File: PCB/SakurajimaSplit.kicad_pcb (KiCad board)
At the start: 2 copper layers, 226 parts, among them J1 SWD, J10 Conn_01x01_Pin, J11 Conn_01x01_Pin, J12 Conn_01x01_Pin, J13 Conn_01x01_Pin, J14 Conn_01x01_Pin, J15 Conn_01x01_Pin, J16 Conn_01x01_Pin, J17 Conn_01x01_Pin, J18 Conn_01x01_Pin, J19 USB-C to Host, J2 USB-C to Right-Half, J20 SWD, J21 Conn_01x01_Pin, J22 Conn_01x01_Pin, J23 Conn_01x01_Pin, J24 Conn_01x01_Pin, J25 Conn_01x01_Pin, J26 Conn_01x01_Pin, J27 Conn_01x01_Pin, J28 Conn_01x01_Pin, J29 Conn_01x01_Pin, J3 Conn_01x01_Pin, J30 Conn_01x01_Pin, J31 Conn_01x01_Pin, J32 Conn_01x01_Pin, J33 Conn_01x01_Pin, J34 Conn_01x01_Pin, J35 Conn_01x01_Pin, J36 Conn_01x01_Pin, J37 Conn_01x01_Pin, J38 Conn_01x01_Pin, J39 USB-C to Right-Half, J4 Conn_01x01_Pin, J5 Conn_01x01_Pin, J6 Conn_01x01_Pin, J7 Conn_01x01_Pin, J8 Conn_01x01_Pin, J9 Conn_01x01_Pin, SW1 SWCLK/BOOT0, SW2 Knob, SW3 SWCLK/BOOT0, SW4 Knob, U1 USBLC6-2SC6, U2 STM32G0B1CBT6, U3 ZJY_M233, U4 TLV76733DRVR, U5 USBLC6-2SC6, U6 STM32G0B1CBT6, U7 ZJY_M233, U8 TLV76733DRVR, U9 USBLC6-2SC6, Y1 8MHz, Y2 8MHz

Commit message: feat(pcb): design rough layout and update schematic accordingly
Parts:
- removed C17, C18, C19: 100nF, Capacitor_SMD:C_0603_1608Metric
- removed C20: TBD, Capacitor_SMD:C_0805_2012Metric
- removed C21, C22: 4.7uF, Capacitor_SMD:C_0805_2012Metric
- removed J10, J11, J12, J13, J14, J32, J33, J34, J38, J4, J5, J6, J7, J8, J9: Conn_01x01_Pin, Connector_Wire:SolderWirePad_1x01_SMD_1x2mm
- removed J39: USB-C to Right-Half, Connector_USB:USB_C_Receptacle_G-Switch_GT-USB-7010ASV
- removed R13: TBD, Resistor_SMD:R_0603_1608Metric
- removed R14, R15, R16, R17, R18, R19: 10k, Resistor_SMD:R_0603_1608Metric
- removed R20: 330R, Resistor_SMD:R_0603_1608Metric
- removed SW3: SWCLK/BOOT0, Button_Switch_SMD:SW_Push_1P1T_XKB_TS-1187A
- removed SW4: Knob, Rotary_Encoder:RotaryEncoder_Alps_EC11E-Switch_Vertical_H20mm
- removed TP3, TP5, TP6: GND, TestPoint:TestPoint_Pad_2.0x2.0mm
- added TP25: Flash_SDO, Hayata_Lib:TestPoint_Pad_Circular_1.3mm, B.Cu at (161.9, 123.8)
- added TP26: Display_SCLK, Hayata_Lib:TestPoint_Pad_Circular_1.3mm, F.Cu at (165.1, 161.1)
- added TP27: Display_SDI, Hayata_Lib:TestPoint_Pad_Circular_1.3mm, F.Cu at (167.5, 161.1)
- added TP28: Flash_SDO, Hayata_Lib:TestPoint_Pad_Circular_1.3mm, F.Cu at (509.5, 111.2)
- added TP29: Display_SCLK, Hayata_Lib:TestPoint_Pad_Circular_1.3mm, F.Cu at (509.5, 114.7)
- added TP30: Display_SDI, Hayata_Lib:TestPoint_Pad_Circular_1.3mm, F.Cu at (509.5, 118.1)
- added U10: ZJY_M233, Hayata_Lib:OLED_SSD1305, F.Cu at (166.5, 133.5)
- added U11: ZJY_M233, Hayata_Lib:OLED_SSD1305, F.Cu at (479.8, 146.6)
- C1, C6, C7: value 100nF -> 20pF; footprint Capacitor_SMD:C_0603_1608Metric -> Capacitor_SMD:C_0402_1005Metric_Pad0.74x0.62mm_HandSolder
- C13: value 20pF -> 100nF; footprint Capacitor_SMD:C_0402_1005Metric_Pad0.74x0.62mm_HandSolder -> Capacitor_SMD:C_0603_1608Metric
- C14: value 20pF -> TBD; footprint Capacitor_SMD:C_0402_1005Metric_Pad0.74x0.62mm_HandSolder -> Capacitor_SMD:C_0805_2012Metric
- C16, C8: value 100nF -> 4.7uF; footprint Capacitor_SMD:C_0603_1608Metric -> Capacitor_SMD:C_0805_2012Metric
- C3: value 20pF -> 4.7uF; footprint Capacitor_SMD:C_0402_1005Metric_Pad0.74x0.62mm_HandSolder -> Capacitor_SMD:C_0805_2012Metric
- C4: value 4.7uF -> 100nF; footprint Capacitor_SMD:C_0805_2012Metric -> Capacitor_SMD:C_0603_1608Metric
- C5, D1, D10, D11, D12, D13, D14, D15, D16, D17, D18, D19, D2, D20, D21, D3, D4, D5, D6, D7, D8, D9, J1: moved to B.Cu
- H1, H2, H3, H4, H5, H6, H7, H8: footprint MountingHole:MountingHole_3.2mm_M3_Pad -> MountingHole:MountingHole_3.2mm_M3_Pad_Via
- J15: value Conn_01x01_Pin -> SWD; footprint Connector_Wire:SolderWirePad_1x01_SMD_1x2mm -> Connector_PinHeader_2.54mm:PinHeader_1x05_P2.54mm_Horizontal
- J20: value SWD -> Conn_01x01_Pin; footprint Connector_PinHeader_2.54mm:PinHeader_1x05_P2.54mm_Horizontal -> Connector_Wire:SolderWirePad_1x01_SMD_1x2mm
- J3: value Conn_01x01_Pin -> VREF+
- J31: value Conn_01x01_Pin -> USB-C to Right-Half; footprint Connector_Wire:SolderWirePad_1x01_SMD_1x2mm -> Connector_USB:USB_C_Receptacle_G-Switch_GT-USB-7010ASV
- MX21, MX40: footprint PCM_marbastlib-mx:SW_MX_1u -> PCM_marbastlib-mx:SW_MX_1.5u
- R3, R4: value 10k -> 5.1k; moved to B.Cu
- R5: value 10k -> 330R
- R6: value 10k -> TBD
- R7, R8: value 10k -> 5.1k
- SW1: footprint Button_Switch_SMD:SW_Push_1P1T_XKB_TS-1187A -> Hayata_Lib:SW_Push_TS-1010B
- SW2: value Knob -> SWCLK/BOOT0; footprint Rotary_Encoder:RotaryEncoder_Alps_EC11E-Switch_Vertical_H20mm -> Hayata_Lib:SW_Push_TS-1010B
- TP1, TP10, TP11, TP12, TP13, TP14, TP15, TP16, TP17, TP2, TP20, TP21, TP22, TP23, TP24, TP4, TP9: footprint TestPoint:TestPoint_Pad_2.0x2.0mm -> Hayata_Lib:TestPoint_Pad_Circular_1.3mm
- TP18: value Display_SCLK -> Flash_SCLK; footprint TestPoint:TestPoint_Pad_2.0x2.0mm -> Hayata_Lib:TestPoint_Pad_Circular_1.3mm
- TP19: value Display_SDI -> Flash_SDI; footprint TestPoint:TestPoint_Pad_2.0x2.0mm -> Hayata_Lib:TestPoint_Pad_Circular_1.3mm
- TP7: value Display_SCLK -> Flash_SCLK; footprint TestPoint:TestPoint_Pad_2.0x2.0mm -> Hayata_Lib:TestPoint_Pad_Circular_1.3mm; moved to B.Cu
- TP8: value Display_SDI -> Flash_SDI; footprint TestPoint:TestPoint_Pad_2.0x2.0mm -> Hayata_Lib:TestPoint_Pad_Circular_1.3mm; moved to B.Cu
- U3: value ZJY_M233 -> W25Q128JVS; footprint Hayata_Lib:OLED_SSD1305 -> Package_SO:SOIC-8_5.3x5.3mm_P1.27mm; moved to B.Cu
- U7: value ZJY_M233 -> W25Q128JVS; footprint Hayata_Lib:OLED_SSD1305 -> Package_SO:SOIC-8_5.3x5.3mm_P1.27mm
- Y1, Y2: footprint Crystal:Crystal_SMD_3225-4Pin_3.2x2.5mm_HandSoldering -> Crystal:Crystal_SMD_3225-4Pin_3.2x2.5mm
- moved SW2 586.0 mm to (504.8, 130.5)
- moved C6 553.4 mm to (507.7, 136.4)
- moved C7 553.4 mm to (507.7, 138.4)
- moved C8 548.6 mm to (503.1, 138.9)
- moved J15 539.9 mm to (499.2, 154.2)
- moved R5 537.6 mm to (494.9, 158.2)
- moved R6 534.7 mm to (494.9, 160.7)
- moved R7 534.7 mm to (494.9, 163.2)
- moved R8 534.7 mm to (494.9, 165.7)
- moved J18 533.3 mm to (499.3, 143.1)
- moved J17 533.1 mm to (496.8, 143.1)
- moved J16 532.9 mm to (494.2, 143.1)
- moved H1 247.4 mm to (196.1, 122.2)
- moved H2 247.4 mm to (196.1, 130.1)
- moved H3 247.4 mm to (196.1, 138.1)
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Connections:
- C1 pad 1: +3.3V -> /Left-Half/HSE_IN
- C1 pad 2: /Left-Half/SWCLK/BOOT0 -> GND
- C12 pad 2: /Right-Half/SWCLK/BOOT0 -> GND
- C13 pad 1: /Right-Half/HSE_IN -> +3.3V
- C14 pad 1: Net-(C14-Pad1) -> Net-(JP3-B)
- C15 pad 1: +3.3V -> +5V
- C16 pad 1: +3.3V -> Net-(D47-A)
- C2 pad 1: /Left-Half/HSE_IN -> Net-(C2-Pad1)
- C3 pad 1: Net-(C3-Pad1) -> +3.3V
- C6 pad 1: /Left-Half/Knob_A -> /Right-Half/HSE_IN
- C7 pad 1: /Left-Half/Knob_B -> Net-(C7-Pad1)
- C8 pad 1: /Left-Half/Knob_SW -> +3.3V
- D43 pad 1: Net-(D43-K) -> GND
- D43 pad 2: /Left-Half/CapsLock -> Net-(D43-A)
- D45 pad 1: Net-(D45-K) -> GND
- D45 pad 2: Net-(D44-A) -> Net-(D45-A)
- D46 pad 1: Net-(D46-K) -> GND
- D46 pad 2: /Right-Half/CapsLock -> Net-(D46-A)
- D48 pad 1: Net-(D48-K) -> GND
- D48 pad 2: Net-(D47-A) -> Net-(D48-A)
- J15 pad 1: Net-(J15-Pin_1) -> +3.3V
- J20 pad 1: +3.3V -> Net-(J20-Pin_1)
- R1 pad 1: Net-(D43-K) -> /Left-Half/CapsLock
- R1 pad 2: GND -> Net-(D43-A)
- R11 pad 1: Net-(D45-K) -> Net-(D44-A)
- R11 pad 2: GND -> Net-(D45-A)
- R12 pad 1: Net-(D46-K) -> Net-(D47-A)
- R12 pad 2: GND -> Net-(D48-A)
- R2 pad 1: Net-(C3-Pad1) -> Net-(C2-Pad1)
- R3 pad 1: Net-(R3-Pad1) -> +3.3V
- R3 pad 2: +3.3V -> /Left-Half/Flash_~{CS}
- R4 pad 1: Net-(R4-Pad1) -> +3.3V
- R4 pad 2: +3.3V -> Net-(U3-~{HOLD}/~{RESET}/IO_{3})
- R5 pad 1: Net-(R5-Pad1) -> /Right-Half/CapsLock
- R5 pad 2: +3.3V -> Net-(D46-A)
- R6 pad 1: /Left-Half/Knob_A -> Net-(C7-Pad1)
- R6 pad 2: Net-(R3-Pad1) -> /Right-Half/HSE_OUT
- R7 pad 1: /Left-Half/Knob_B -> +3.3V
- R7 pad 2: Net-(R4-Pad1) -> /Right-Half/Flash_~{CS}
- R8 pad 1: /Left-Half/Knob_SW -> +3.3V
- R8 pad 2: Net-(R5-Pad1) -> Net-(U7-~{HOLD}/~{RESET}/IO_{3})
- TP18 pad 1: /Right-Half/Display_SCLK -> /Right-Half/Flash_SCLK
- TP19 pad 1: /Right-Half/Display_SDI -> /Right-Half/Flash_SDI
- TP20 pad 1: VBUS -> Net-(JP3-B)
- TP7 pad 1: /Left-Half/Display_SCLK -> /Left-Half/Flash_SCLK
- TP8 pad 1: /Left-Half/Display_SDI -> /Left-Half/Flash_SDI
- TP9 pad 1: VBUS -> Net-(JP1-B)
- U2 pad 1: /Left-Half/Knob_A -> /Left-Half/Display_~{CS}
- U2 pad 11: Net-(J4-Pin_1) -> unconnected-(U2-PA0-Pad11)
- U2 pad 12: Net-(J5-Pin_1) -> unconnected-(U2-PA1-Pad12)
- U2 pad 15: Net-(J6-Pin_1) -> /Left-Half/CapsLock
- U2 pad 16: Net-(J7-Pin_1) -> unconnected-(U2-PA5-Pad16)
- U2 pad 17: Net-(J8-Pin_1) -> unconnected-(U2-PA6-Pad17)
- U2 pad 18: Net-(J9-Pin_1) -> unconnected-(U2-PA7-Pad18)
- U2 pad 19: Net-(J16-Pin_1) -> unconnected-(U2-PB0-Pad19)
- U2 pad 2: /Left-Half/Knob_B -> /Left-Half/Display_~{RST}
- U2 pad 20: /Left-Half/CapsLock -> unconnected-(U2-PB1-Pad20)
- U2 pad 21: /Left-Half/Display_DC -> unconnected-(U2-PB2-Pad21)
- U2 pad 22: /Left-Half/Display_~{RST} -> unconnected-(U2-PB10-Pad22)
- U2 pad 23: /Left-Half/Display_~{CS} -> unconnected-(U2-PB11-Pad23)
- U2 pad 24: /Left-Half/Display_~{EN} -> unconnected-(U2-PB12-Pad24)
- U2 pad 25: /Left-Half/Display_SCLK -> /Left-Half/COL0
- U2 pad 26: Net-(J18-Pin_1) -> /Left-Half/COL1
- U2 pad 27: /Left-Half/Display_SDI -> /Left-Half/COL2
- U2 pad 28: Net-(J10-Pin_1) -> /Left-Half/COL3
- U2 pad 29: Net-(J11-Pin_1) -> /Left-Half/COL4
- U2 pad 3: /Left-Half/Knob_SW -> /Left-Half/Display_DC
- U2 pad 30: Net-(J12-Pin_1) -> /Left-Half/COL5
- U2 pad 31: Net-(J13-Pin_1) -> unconnected-(U2-PC7-Pad31)
- U2 pad 32: Net-(J14-Pin_1) -> unconnected-(U2-PA10/UCPD1_DBCC2-Pad32)
- U2 pad 37: Net-(J15-Pin_1) -> /Left-Half/ROW0
- U2 pad 38: /Left-Half/ROW0 -> /Left-Half/ROW1
- U2 pad 39: /Left-Half/ROW1 -> /Left-Half/ROW2
- U2 pad 40: /Left-Half/ROW2 -> /Left-Half/ROW3
- U2 pad 41: /Left-Half/ROW3 -> /Left-Half/Flash_~{CS}
- U2 pad 42: Net-(J17-Pin_1) -> /Left-Half/Flash_SCLK
- U2 pad 43: /Left-Half/COL0 -> /Left-Half/Flash_SDO
- U2 pad 44: /Left-Half/COL1 -> /Left-Half/Flash_SDI
- U2 pad 45: /Left-Half/COL2 -> unconnected-(U2-PB6-Pad45)
- U2 pad 46: /Left-Half/COL3 -> /Left-Half/Display_SDI
- U2 pad 47: /Left-Half/COL4 -> /Left-Half/Display_SCLK
- U2 pad 48: /Left-Half/COL5 -> /Left-Half/Display_~{EN}
- U3 pad 1: GND -> /Left-Half/Flash_~{CS}
- U3 pad 2: +3.3V -> /Left-Half/Flash_SDO
- U3 pad 3: /Left-Half/Display_SCLK -> Net-(U3-~{HOLD}/~{RESET}/IO_{3})
- U3 pad 4: /Left-Half/Display_SDI -> GND
- U3 pad 5: /Left-Half/Display_~{RST} -> /Left-Half/Flash_SDI
- U3 pad 6: /Left-Half/Display_DC -> /Left-Half/Flash_SCLK
- U3 pad 7: /Left-Half/Display_~{CS} -> Net-(U3-~{HOLD}/~{RESET}/IO_{3})
- U3 pad 8: /Left-Half/Display_~{EN} -> +3.3V
- U6 pad 1: /Right-Half/Knob_A -> Net-(J27-Pin_1)
- U6 pad 11: Net-(J22-Pin_1) -> Net-(J17-Pin_1)
- U6 pad 12: Net-(J23-Pin_1) -> Net-(J18-Pin_1)
- U6 pad 15: Net-(J24-Pin_1) -> /Right-Half/Flash_~{CS}
- U6 pad 16: Net-(J25-Pin_1) -> /Right-Half/Flash_SCLK
- U6 pad 17: Net-(J26-Pin_1) -> /Right-Half/Flash_SDO
- U6 pad 18: Net-(J27-Pin_1) -> /Right-Half/Flash_SDI
- U6 pad 19: Net-(J36-Pin_1) -> Net-(J35-Pin_1)
- U6 pad 2: /Right-Half/Knob_B -> Net-(J28-Pin_1)
- U6 pad 26: Net-(J38-Pin_1) -> Net-(J37-Pin_1)
- U6 pad 28: Net-(J28-Pin_1) -> Net-(J20-Pin_1)
- U6 pad 29: Net-(J30-Pin_1) -> Net-(J22-Pin_1)
- U6 pad 3: /Right-Half/Knob_SW -> Net-(J29-Pin_1)
- U6 pad 30: Net-(J31-Pin_1) -> Net-(J23-Pin_1)
- U6 pad 31: Net-(J33-Pin_1) -> Net-(J25-Pin_1)
- U6 pad 32: Net-(J34-Pin_1) -> Net-(J26-Pin_1)
- U6 pad 33: Net-(J29-Pin_1) -> Net-(J21-Pin_1)
- U6 pad 34: Net-(J32-Pin_1) -> Net-(J24-Pin_1)
- U6 pad 37: Net-(J35-Pin_1) -> Net-(J30-Pin_1)
- U6 pad 42: Net-(J37-Pin_1) -> Net-(J36-Pin_1)
- U6 pad 5: Net-(J21-Pin_1) -> Net-(J16-Pin_1)
- U7 pad 1: GND -> /Right-Half/Flash_~{CS}
- U7 pad 2: +3.3V -> /Right-Half/Flash_SDO
- U7 pad 3: /Right-Half/Display_SCLK -> Net-(U7-~{HOLD}/~{RESET}/IO_{3})
- U7 pad 4: /Right-Half/Display_SDI -> GND
- U7 pad 5: /Right-Half/Display_~{RST} -> /Right-Half/Flash_SDI
- U7 pad 6: /Right-Half/Display_DC -> /Right-Half/Flash_SCLK
- U7 pad 7: /Right-Half/Display_~{CS} -> Net-(U7-~{HOLD}/~{RESET}/IO_{3})
- U7 pad 8: /Right-Half/Display_~{EN} -> +3.3V
- U9 pad 1: Net-(J39-D--PadA7) -> Net-(J31-D--PadA7)
- U9 pad 3: Net-(J39-D+-PadA6) -> Net-(J31-D+-PadA6)
- Y1 pad 3: Net-(C3-Pad1) -> Net-(C2-Pad1)
- Y2 pad 3: Net-(C14-Pad1) -> Net-(C7-Pad1)
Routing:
- net VBUS: track 0.00 -> 7.38 mm
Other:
- board outline added: 146.1 x 113.5 mm

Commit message: feat(pcb): finish designing rough layout and update schematic
- Removed unused MCU pads
- Removed some GND testpoints
- Updated MCU connections based on PCB layout and MCU orientation
- Updated key matrix layout for a less aggressive one which feels more
  comfortable and more visually pleasing
- Re-annotated schematic
- Finished rough component placement
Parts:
- removed J16, J17, J18, J20, J21, J22, J23, J24, J25, J26, J27, J28, J29, J30, J35, J36, J37: Conn_01x01_Pin, Connector_Wire:SolderWirePad_1x01_SMD_1x2mm
- removed TP15, TP16, TP17: GND, Hayata_Lib:TestPoint_Pad_Circular_1.3mm
- added J4: VREF+, Connector_Wire:SolderWirePad_1x01_SMD_1x2mm, F.Cu at (247.7, 72.2)
- C5, R3, R4, TP25, TP7, TP8, U3: moved to F.Cu
- D22, D23, D24, D25, D26, D27, D28, D29, D30, D31, D32, D33, D34, D35, D36, D37, D38, D39, D40, D41, D42, J15, TP26, TP27, TP29, TP30: moved to B.Cu
- moved J31 287.5 mm to (252.4, 155.6), turned to -90 degrees
- moved D48 285.9 mm to (249.2, 140.5), turned to 90 degrees
- moved D47 281.6 mm to (258.8, 134.9), turned to 90 degrees
- moved L2 280.7 mm to (259.6, 139.7), turned to 90 degrees
- moved C16 279.9 mm to (255.6, 131.8), turned to 180 degrees
- moved R12 279.8 mm to (250.8, 140.5), turned to 90 degrees
- moved C14 279.7 mm to (255.6, 140.5), turned to 180 degrees
- moved C15 279.6 mm to (255.6, 138.1), turned to 180 degrees
- moved U9 279.0 mm to (261.1, 152.4), turned to 90 degrees
- moved U8 275.7 mm to (255.2, 134.9), turned to -90 degrees
- moved TP22 275.4 mm to (251.6, 129.4), turned to 180 degrees
- moved TP21 275.3 mm to (251.6, 134.1), turned to 180 degrees
- moved JP3 274.9 mm to (256.4, 143.7), turned to 90 degrees
- moved JP4 274.5 mm to (256.4, 128.6), turned to 90 degrees
- moved TP20 267.9 mm to (259.6, 143.7), turned to 180 degrees
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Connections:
- U2 pad 24: unconnected-(U2-PB12-Pad24) -> /Left-Half/Flash_~{CS}
- U2 pad 25: /Left-Half/COL0 -> /Left-Half/Flash_SCLK
- U2 pad 26: /Left-Half/COL1 -> /Left-Half/Flash_SDO
- U2 pad 27: /Left-Half/COL2 -> /Left-Half/Flash_SDI
- U2 pad 28: /Left-Half/COL3 -> /Left-Half/COL0
- U2 pad 29: /Left-Half/COL4 -> unconnected-(U2-PA9/UCPD1_DBCC1-Pad29)
- U2 pad 30: /Left-Half/COL5 -> unconnected-(U2-PC6-Pad30)
- U2 pad 37: /Left-Half/ROW0 -> /Left-Half/COL1
- U2 pad 38: /Left-Half/ROW1 -> /Left-Half/COL2
- U2 pad 39: /Left-Half/ROW2 -> /Left-Half/COL3
- U2 pad 40: /Left-Half/ROW3 -> /Left-Half/COL4
- U2 pad 41: /Left-Half/Flash_~{CS} -> /Left-Half/COL5
- U2 pad 42: /Left-Half/Flash_SCLK -> /Left-Half/Display_SCLK
- U2 pad 43: /Left-Half/Flash_SDO -> /Left-Half/ROW0
- U2 pad 44: /Left-Half/Flash_SDI -> /Left-Half/Display_SDI
- U2 pad 45: unconnected-(U2-PB6-Pad45) -> /Left-Half/ROW1
- U2 pad 46: /Left-Half/Display_SDI -> /Left-Half/ROW2
- U2 pad 47: /Left-Half/Display_SCLK -> /Left-Half/ROW3
- U6 pad 1: Net-(J27-Pin_1) -> unconnected-(U6-PC13-Pad1)
- U6 pad 11: Net-(J17-Pin_1) -> unconnected-(U6-PA0-Pad11)
- U6 pad 12: Net-(J18-Pin_1) -> unconnected-(U6-PA1-Pad12)
- U6 pad 15: /Right-Half/Flash_~{CS} -> /Right-Half/ROW3
- U6 pad 16: /Right-Half/Flash_SCLK -> /Right-Half/Display_SCLK
- U6 pad 17: /Right-Half/Flash_SDO -> /Right-Half/Display_~{EN}
- U6 pad 18: /Right-Half/Flash_SDI -> /Right-Half/Display_SDI
- U6 pad 19: Net-(J35-Pin_1) -> /Right-Half/Display_~{CS}
- U6 pad 2: Net-(J28-Pin_1) -> unconnected-(U6-PC14-Pad2)
- U6 pad 20: /Right-Half/CapsLock -> /Right-Half/Display_~{RST}
- U6 pad 22: /Right-Half/Display_~{RST} -> /Right-Half/ROW2
- U6 pad 23: /Right-Half/Display_~{CS} -> /Right-Half/ROW1
- U6 pad 24: /Right-Half/Display_~{EN} -> /Right-Half/ROW0
- U6 pad 25: /Right-Half/Display_SCLK -> /Right-Half/COL5
- U6 pad 26: Net-(J37-Pin_1) -> /Right-Half/COL4
- U6 pad 27: /Right-Half/Display_SDI -> /Right-Half/COL3
- U6 pad 28: Net-(J20-Pin_1) -> /Right-Half/COL2
- U6 pad 29: Net-(J22-Pin_1) -> /Right-Half/COL1
- U6 pad 3: Net-(J29-Pin_1) -> unconnected-(U6-PC15-Pad3)
- U6 pad 30: Net-(J23-Pin_1) -> /Right-Half/COL0
- U6 pad 31: Net-(J25-Pin_1) -> unconnected-(U6-PC7-Pad31)
- U6 pad 32: Net-(J26-Pin_1) -> unconnected-(U6-PA10/UCPD1_DBCC2-Pad32)
- U6 pad 33: Net-(J21-Pin_1) -> unconnected-(U6-PA9/PA11-Pad33)
- U6 pad 34: Net-(J24-Pin_1) -> unconnected-(U6-PA10/PA12-Pad34)
- U6 pad 37: Net-(J30-Pin_1) -> unconnected-(U6-PA15-Pad37)
- U6 pad 38: /Right-Half/ROW0 -> unconnected-(U6-PD0-Pad38)
- U6 pad 39: /Right-Half/ROW1 -> unconnected-(U6-PD1-Pad39)
- U6 pad 40: /Right-Half/ROW2 -> unconnected-(U6-PD2-Pad40)
- U6 pad 41: /Right-Half/ROW3 -> unconnected-(U6-PD3-Pad41)
- U6 pad 42: Net-(J36-Pin_1) -> unconnected-(U6-PB3-Pad42)
- U6 pad 43: /Right-Half/COL0 -> unconnected-(U6-PB4-Pad43)
- U6 pad 44: /Right-Half/COL1 -> /Right-Half/Flash_~{CS}
- U6 pad 45: /Right-Half/COL2 -> /Right-Half/Flash_SDO
- U6 pad 46: /Right-Half/COL3 -> /Right-Half/Flash_SDI
- U6 pad 47: /Right-Half/COL4 -> /Right-Half/Flash_SCLK
- U6 pad 48: /Right-Half/COL5 -> /Right-Half/CapsLock
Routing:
- net +3.3V: track 0.00 -> 15.9 mm
- net Net-(J31-D+-PadA6): track 0.00 -> 8.04 mm
- net Net-(J31-D--PadA7): track 0.00 -> 5.75 mm
- net /Left-Half/Flash_SCLK: track 0.00 -> 5.11 mm
- net VBUS: track 7.38 -> 12.4 mm
- net /Left-Half/Flash_SDI: track 0.00 -> 3.02 mm
- net /Left-Half/Flash_SDO: track 0.00 -> 1.83 mm
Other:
- board size 146.1 x 113.5 mm -> 347.7 x 112.4 mm
- board text added: "SakurajimaSplit"
- board text added: "by HayataSama"

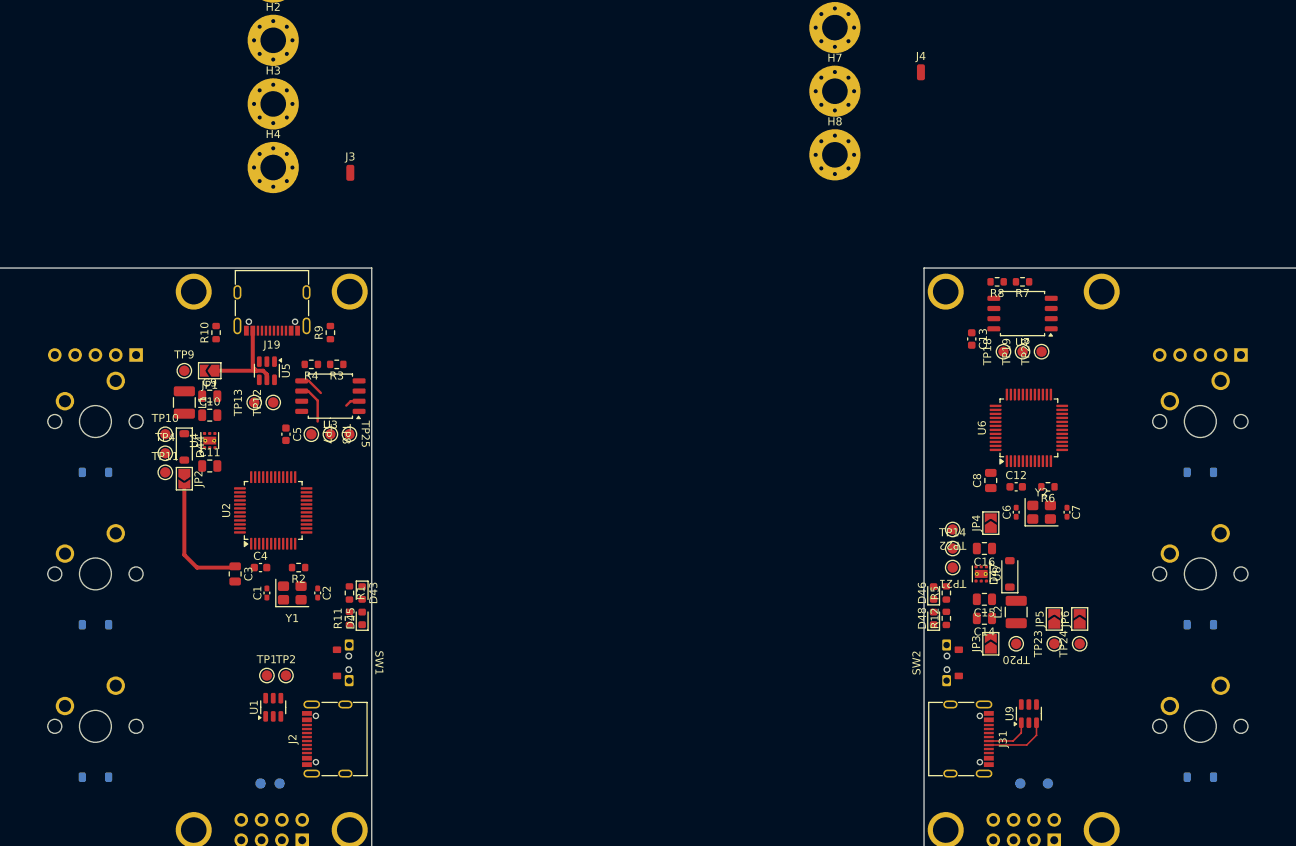
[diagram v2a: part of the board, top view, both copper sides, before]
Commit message: feat(pcb): fine tune pcb layout
- fine tuned pcb layout
- swaped TX and RX pins of right half for better routing
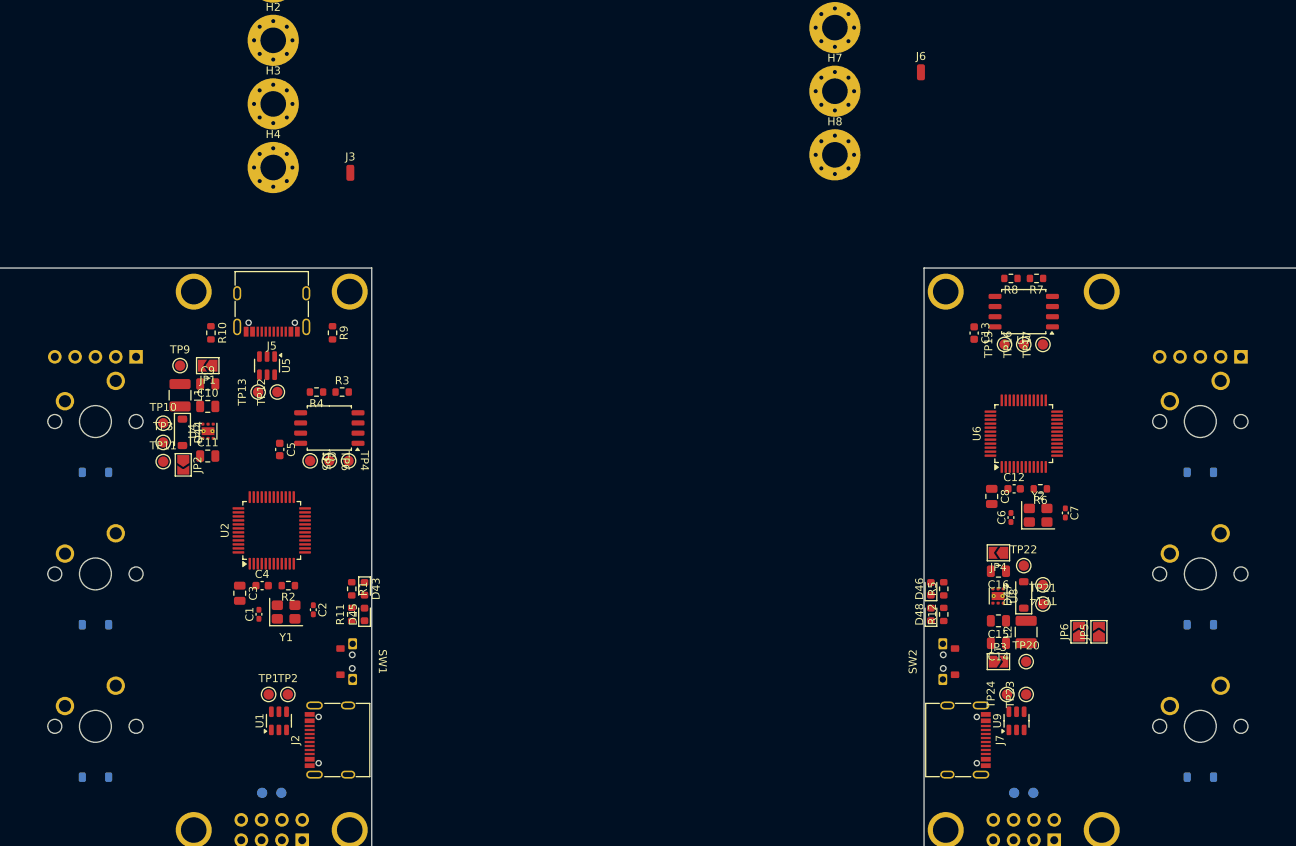
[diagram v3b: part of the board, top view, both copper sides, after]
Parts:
- moved TP21 12.2 mm to (262.9, 138.7), turned to 0 degrees
- moved TP14 12.2 mm to (262.9, 136.3), turned to 180 degrees
- moved TP24 11.1 mm to (258.4, 150.0)
- moved TP22 9.96 mm to (260.5, 133.9), turned to 0 degrees
- moved TP23 7.24 mm to (260.8, 150.0)
- moved JP5 5.81 mm to (269.9, 142.2)
- moved TP4 5.72 mm to (176.1, 120.8)
- moved TP5 4.18 mm to (171.3, 120.8)
- moved TP6 4.17 mm to (173.7, 120.8)
- moved U3 3.99 mm to (173.7, 116.7)
- moved JP4 3.83 mm to (257.3, 132.3), turned to 180 degrees
- moved C14 3.57 mm to (257.3, 143.6)
- moved R3 3.52 mm to (175.3, 112.2), turned to 0 degrees
- moved R4 3.52 mm to (172.1, 112.2)
- moved U8 3.48 mm to (257.3, 137.7)
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- renumbered J15 to J4, J19 to J5, J4 to J6, J31 to J7, TP18 to TP15, TP19 to TP16, TP28 to TP17, TP29 to TP18, TP30 to TP19, TP4 to TP3, TP7 to TP4, TP8 to TP5, TP25 to TP6, TP26 to TP7, TP27 to TP8
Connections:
- J7 pad A6: Net-(J31-D+-PadA6) -> Net-(J7-D+-PadA6)
- J7 pad A7: Net-(J31-D--PadA7) -> Net-(J7-D--PadA7)
- J7 pad B6: Net-(J31-D+-PadA6) -> Net-(J7-D+-PadA6)
- J7 pad B7: Net-(J31-D--PadA7) -> Net-(J7-D--PadA7)
- U9 pad 1: Net-(J31-D--PadA7) -> Net-(J7-D+-PadA6)
- U9 pad 3: Net-(J31-D+-PadA6) -> Net-(J7-D--PadA7)
- U9 pad 4: Net-(JP6-A) -> Net-(JP5-A)
- U9 pad 6: Net-(JP5-A) -> Net-(JP6-A)
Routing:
- net +3.3V: track 15.9 -> 0.00 mm
- net VBUS: track 12.4 -> 0.00 mm
- net Net-(J31-D+-PadA6): track 8.04 -> 0.00 mm
- net Net-(J31-D--PadA7): track 5.75 -> 0.00 mm
- net /Left-Half/Flash_SCLK: track 5.11 -> 0.00 mm
- net /Left-Half/Flash_SDI: track 3.02 -> 0.00 mm
- net /Left-Half/Flash_SDO: track 1.83 -> 0.00 mm

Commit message: feat(pcb): route left half
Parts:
- D22, D23, D24, D25, D26, D27, D28, D29, D30, D31, D32, D33, D34, D35, D36, D37, D38, D39, D40, D41, D42: moved to F.Cu
- J3: moved to B.Cu
- moved J3 47.0 mm to (165.8, 130.6), turned to 180 degrees
- moved D40 2.54 mm to (255.3, 193.3), turned to 38 degrees
- moved D20 2.54 mm to (153.7, 177.6)
- moved D22 2.54 mm to (285.1, 122.3), turned to 90 degrees
- moved D23 2.54 mm to (304.2, 117.5), turned to 90 degrees
- moved D26 2.54 mm to (361.3, 122.3), turned to 90 degrees
- moved D27 2.54 mm to (380.4, 122.3), turned to 90 degrees
- moved D28 2.54 mm to (285.1, 141.3), turned to 90 degrees
- moved D29 2.54 mm to (304.2, 136.6), turned to 90 degrees
- moved D32 2.54 mm to (361.3, 141.3), turned to 90 degrees
- moved D33 2.54 mm to (380.4, 141.3), turned to 90 degrees
- moved D34 2.54 mm to (285.1, 160.4), turned to 90 degrees
- moved D35 2.54 mm to (304.2, 155.6), turned to 90 degrees
- moved D38 2.54 mm to (361.3, 160.4), turned to 90 degrees
- moved D39 2.54 mm to (380.4, 160.4), turned to 90 degrees
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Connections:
- U2 pad 1: /Left-Half/Display_~{CS} -> /Left-Half/Display_~{EN}
- U2 pad 48: /Left-Half/Display_~{EN} -> /Left-Half/Display_~{CS}
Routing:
- net /Left-Half/COL0: track 0.00 -> 192.8 mm, vias 0 -> 1
- net /Left-Half/COL3: track 0.00 -> 170.0 mm, vias 0 -> 1
- net /Left-Half/COL1: track 0.00 -> 168.0 mm, vias 0 -> 1
- net /Left-Half/COL4: track 0.00 -> 153.9 mm, vias 0 -> 1
- net /Left-Half/COL5: track 0.00 -> 151.5 mm, vias 0 -> 1
- net /Left-Half/ROW2: track 0.00 -> 150.1 mm, vias 0 -> 1
- net /Left-Half/COL2: track 0.00 -> 147.7 mm, vias 0 -> 1
- net +3.3V: track 0.00 -> 134.9 mm, vias 0 -> 4
- net /Left-Half/ROW1: track 0.00 -> 131.6 mm, vias 0 -> 1
- net /Left-Half/ROW0: track 0.00 -> 126.2 mm, vias 0 -> 1
- net /Left-Half/ROW3: track 0.00 -> 126.1 mm, vias 0 -> 1
- net VBUS: track 0.00 -> 92.3 mm, vias 0 -> 4
- net /Left-Half/SWCLK/BOOT0: track 0.00 -> 69.6 mm, vias 0 -> 4
- net /Left-Half/Display_SCLK: track 0.00 -> 50.3 mm, vias 0 -> 1
- net /Left-Half/NRST: track 0.00 -> 48.2 mm, vias 0 -> 1
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- added copper zone on B.Cu, net GND
- added copper zone on F.Cu, net GND
- added copper zone on F.Cu, net VBUS

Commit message: feat(pcb): route right half
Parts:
- D22, D23, D24, D25, D26, D27, D28, D29, D30, D31, D32, D33, D34, D35, D36, D37, D38, D39, D40, D41, D42, J6: moved to B.Cu
- moved J6 57.1 mm to (214.2, 118.5), turned to 180 degrees
- moved JP5 51.4 mm to (219.1, 149.9), turned to 0 degrees
- moved JP6 48.6 mm to (219.1, 147.4), turned to 0 degrees
- moved D23 45.7 mm to (258.5, 117.5)
- moved D27 45.7 mm to (334.7, 122.2)
- moved D29 45.7 mm to (258.5, 136.5)
- moved D33 45.7 mm to (334.7, 141.3)
- moved D35 45.7 mm to (258.5, 155.6)
- moved D39 45.7 mm to (334.7, 160.3)
- moved D42 45.7 mm to (261.0, 179.4)
- moved MX24 45.7 mm to (275.0, 101.5)
- moved MX25 45.7 mm to (294.1, 111.1)
- moved MX30 45.7 mm to (275.0, 120.6)
- moved MX31 45.7 mm to (294.1, 130.1)
- moved MX36 45.7 mm to (275.0, 139.7)
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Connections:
- U6 pad 17: /Right-Half/Display_~{EN} -> /Right-Half/Display_~{CS}
- U6 pad 19: /Right-Half/Display_~{CS} -> /Right-Half/Display_~{EN}
- U6 pad 25: /Right-Half/COL5 -> /Right-Half/COL0
- U6 pad 26: /Right-Half/COL4 -> /Right-Half/COL1
- U6 pad 27: /Right-Half/COL3 -> /Right-Half/COL2
- U6 pad 28: /Right-Half/COL2 -> /Right-Half/COL3
- U6 pad 29: /Right-Half/COL1 -> /Right-Half/COL4
- U6 pad 30: /Right-Half/COL0 -> /Right-Half/COL5
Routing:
- net /Right-Half/COL5: track 0.00 -> 173.0 mm, vias 0 -> 1
- net /Right-Half/ROW2: track 0.00 -> 171.9 mm, vias 0 -> 1
- net /Right-Half/COL4: track 0.00 -> 153.5 mm, vias 0 -> 1
- net /Right-Half/ROW1: track 0.00 -> 153.1 mm, vias 0 -> 1
- net +3.3V: track 134.9 -> 280.9 mm
- net /Right-Half/COL2: track 0.00 -> 142.7 mm, vias 0 -> 1
- net /Right-Half/ROW0: track 0.00 -> 135.1 mm, vias 0 -> 1
- net /Right-Half/COL3: track 0.00 -> 131.3 mm, vias 0 -> 1
- net /Right-Half/ROW3: track 0.00 -> 130.4 mm, vias 0 -> 1
- net /Right-Half/COL1: track 0.00 -> 124.7 mm, vias 0 -> 1
- net /Right-Half/COL0: track 0.00 -> 102.6 mm, vias 0 -> 1
- net /Right-Half/SWCLK/BOOT0: track 0.00 -> 67.0 mm, vias 0 -> 2
- net /Right-Half/Display_~{RST}: track 0.00 -> 65.2 mm, vias 0 -> 1
- net /Right-Half/Display_SCLK: track 0.00 -> 64.3 mm, vias 0 -> 1
- net /Right-Half/Display_DC: track 0.00 -> 63.4 mm, vias 0 -> 1
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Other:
- board size 347.7 x 112.4 mm -> 302 x 112.4 mm
